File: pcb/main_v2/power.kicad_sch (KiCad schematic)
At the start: 33 parts, among them IC201 AP22811AW5-7, J201 USB_A, SW201 SW_DIP_x01, U201 LT3042xMSE

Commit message: updated schematic after review
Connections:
- net CONN-1 renamed Power Enable
- net CONN-2 renamed Power Faulty
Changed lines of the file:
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@@
 	(wire
 		(pts
-			(xy 193.04 48.26) (xy 193.04 80.01)
+			(xy 193.04 48.26) (xy 193.04 85.09)
 		)
 		(stroke
@@
 		(pts
 			(xy 43.18 128.27) (xy 43.18 138.43)
-		)
-		(stroke
-			(width 0)
-			(type default)
-		)
-	)
-	(wire
-		(pts
-			(xy 193.04 80.01) (xy 193.04 82.55)
 		)
 		(stroke
@@
 				)
 				(justify left)
-			)
-		)
-	)
-	(global_label "CONN-1"
-		(shape input)
-		(at 144.78 48.26 180)
-		(fields_autoplaced yes)
-		(effects
-			(font
-				(size 1.27 1.27)
-			)
-			(justify right)
-		)
-		(property "Intersheetrefs" "${INTERSHEET_REFS}"
-			(at 133.7514 48.26 0)
-			(hide yes)
-			(show_name no)
-			(do_not_autoplace no)
-			(effects
-				(font
-					(size 1.27 1.27)
-				)
-				(justify right)
 			)
 		)
@@
 		)
 	)
-	(global_label "CONN-2"
+	(hierarchical_label "Power Enable"
 		(shape input)
-		(at 193.04 82.55 270)
+		(at 144.78 48.26 180)
 		(fields_autoplaced yes)
 		(effects
@@
 			(justify right)
 		)
-		(property "Intersheetrefs" "${INTERSHEET_REFS}"
-			(at 193.04 93.5786 90)
-			(hide yes)
-			(show_name no)
-			(do_not_autoplace no)
-			(effects
-				(font
-					(size 1.27 1.27)
+		(property "Netzklasse" "Default"
+			(at 144.78 49.53 0)
+			(show_name no)
+			(do_not_autoplace no)
+			(effects
+				(font
+					(size 1.27 1.27)
+					(italic yes)
 				)
 				(justify right)
 			)
 		)
+	)
+	(hierarchical_label "Power Faulty"
+		(shape input)
+		(at 193.04 85.09 270)
+		(fields_autoplaced yes)
+		(effects
+			(font
+				(size 1.27 1.27)
+			)
+			(justify right)
+		)
+		(property "Netzklasse" "Default"
+			(at 194.31 85.09 90)
+			(show_name no)
+			(do_not_autoplace no)
+			(effects
+				(font
+					(size 1.27 1.27)
+					(italic yes)
+				)
+				(justify right)
+			)
+		)
+	)
+	(netclass_flag ""
+		(length 2.54)
+		(shape diamond)
+		(at 194.31 43.18 0)
+		(fields_autoplaced yes)
+		(effects
+			(font
+				(size 1.27 1.27)
+			)
+			(justify left bottom)
+		)
+		(property "Netzklasse" "Power"
+			(at 195.5165 40.64 0)
+			(show_name no)
+			(do_not_autoplace no)
+			(effects
+				(font
+					(size 1.27 1.27)
+				)
+				(justify left)
+			)
+		)
+		(property "Component Class" ""
+			(at 6.35 20.32 0)
+			(show_name no)
+			(do_not_autoplace no)
+			(effects
+				(font
+					(size 1.27 1.27)
+					(italic yes)
+				)
+			)
+		)
+	)
+	(netclass_flag ""
+		(length 2.54)
+		(shape diamond)
+		(at 173.99 128.27 0)
+		(fields_autoplaced yes)
+		(effects
+			(font
+				(size 1.27 1.27)
+			)
+			(justify left bottom)
+		)
+		(property "Netzklasse" "Power"
+			(at 175.1965 125.73 0)
+			(show_name no)
+			(do_not_autoplace no)
+			(effects
+				(font
+					(size 1.27 1.27)
+				)
+				(justify left)
+			)
+		)
+		(property "Component Class" ""
+			(at -13.97 105.41 0)
+			(show_name no)
+			(do_not_autoplace no)
+			(effects
+				(font
+					(size 1.27 1.27)
+					(italic yes)
+				)
+			)
+		)
+	)
+	(netclass_flag ""
+		(length 2.54)
+		(shape diamond)
+		(at 134.62 43.18 0)
+		(fields_autoplaced yes)
+		(effects
+			(font
+				(size 1.27 1.27)
+			)
+			(justify left bottom)
+		)
+		(property "Netzklasse" "Power"
+			(at 135.8265 40.64 0)
+			(show_name no)
+			(do_not_autoplace no)
+			(effects
+				(font
+					(size 1.27 1.27)
+				)
+				(justify left)
+			)
+		)
+		(property "Component Class" ""
+			(at -53.34 20.32 0)
+			(show_name no)
+			(do_not_autoplace no)
+			(effects
+				(font
+					(size 1.27 1.27)
+					(italic yes)
+				)
+			)
+		)

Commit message: added new osci
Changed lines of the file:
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@@
-	(wire
-		(pts
-			(xy 90.17 39.37) (xy 90.17 43.18)
-		)
-		(stroke
-			(width 0)
-			(type default)
-		)
-	)
 	(wire
 		(pts
@@
 		)
 	)
-	(global_label "USB Power"
-		(shape input)
-		(at 90.17 39.37 90)
-		(fields_autoplaced yes)
+	(label "USB Power"
+		(at 86.36 43.18 90)
 		(effects
 			(font
 				(size 1.27 1.27)
 			)
-			(justify left)
-		)
-		(property "Intersheetrefs" "${INTERSHEET_REFS}"
-			(at 90.17 25.9829 90)
-			(hide yes)
-			(show_name no)
-			(do_not_autoplace no)
-			(effects
-				(font
-					(size 1.27 1.27)
-				)
-				(justify left)
-			)
-		)
-		(property "Net Class" "Power"
-			(at 94.0118 39.37 90)
-			(show_name no)
-			(do_not_autoplace no)
-			(effects
-				(font
-					(size 1.27 1.27)
-				)
-				(justify left)
-			)
-		)
-	)
-	(global_label "USB Power"
-		(shape input)
+			(justify left bottom)
+		)
+	)
+	(label "USB Power"
 		(at 212.09 80.01 0)
-		(fields_autoplaced yes)
 		(effects
 			(font
 				(size 1.27 1.27)
 			)
-			(justify left)
-		)
-		(property "Intersheetrefs" "${INTERSHEET_REFS}"
-			(at 225.4771 80.01 0)
-			(hide yes)
-			(show_name no)
-			(do_not_autoplace no)
-			(effects
-				(font
-					(size 1.27 1.27)
-				)
-				(justify left)
-			)
+			(justify left bottom)
 		)
 	)
@@
 			)
 		)
+	)
+	(netclass_flag ""
+		(length 2.54)
+		(shape diamond)
+		(at 69.85 43.18 0)
+		(fields_autoplaced yes)
+		(effects
+			(font
+				(size 1.27 1.27)
+			)
+			(justify left bottom)
+		)
+		(property "Net Class" "Power"
+			(at 71.0565 40.64 0)
+			(show_name no)
+			(do_not_autoplace no)
+			(effects
+				(font
+					(size 1.27 1.27)
+				)
+				(justify left)
+			)
+		)
+		(property "Component Class" ""
+			(at 60.96 35.56 0)
+			(show_name no)
+			(do_not_autoplace no)
+			(effects
+				(font
+					(size 1.27 1.27)
+					(italic yes)
+				)
+			)
+		)

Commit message: updated schematic
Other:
- moved on the sheet: R202, TP202
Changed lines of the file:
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@@
+	)
+	(junction
+		(at 193.04 80.01)
+		(diameter 0)
+		(color 0 0 0 0)
+	)
+	(junction
+		(at 204.47 52.07)
+		(diameter 0)
+		(color 0 0 0 0)
+	)
+	(junction
+		(at 132.08 128.27)
+		(diameter 0)
+		(color 0 0 0 0)
+	)
+	(junction
+		(at 66.04 43.18)
+		(diameter 0)
+		(color 0 0 0 0)
+	)
+	(junction
+		(at 96.52 128.27)
+		(diameter 0)
+		(color 0 0 0 0)
+	)
+	(junction
+		(at 226.06 43.18)
+		(diameter 0)
+		(color 0 0 0 0)
+	)
+	(junction
+		(at 96.52 135.89)
+		(diameter 0)
+		(color 0 0 0 0)
+	)
+	(junction
+		(at 162.56 48.26)
+		(diameter 0)
+		(color 0 0 0 0)
+	)
+	(junction
+		(at 161.29 137.16)
+		(diameter 0)
+		(color 0 0 0 0)
 	)
 	(junction
@@
 	)
 	(junction
-		(at 193.04 80.01)
+		(at 116.84 128.27)
 		(diameter 0)
 		(color 0 0 0 0)
 	)
 	(junction
-		(at 204.47 52.07)
+		(at 157.48 43.18)
 		(diameter 0)
 		(color 0 0 0 0)
 	)
 	(junction
-		(at 132.08 128.27)
+		(at 96.52 147.32)
 		(diameter 0)
 		(color 0 0 0 0)
 	)
 	(junction
-		(at 66.04 43.18)
+		(at 161.29 128.27)
 		(diameter 0)
 		(color 0 0 0 0)
 	)
 	(junction
-		(at 96.52 128.27)
+		(at 53.34 67.31)
+		(diameter 0)
+		(color 0 0 0 0)
+	)
+	(junction
+		(at 132.08 43.18)
 		(diameter 0)
 		(color 0 0 0 0)
@@
 	)
 	(junction
-		(at 226.06 43.18)
-		(diameter 0)
-		(color 0 0 0 0)
-	)
-	(junction
-		(at 96.52 135.89)
-		(diameter 0)
-		(color 0 0 0 0)
-	)
-	(junction
-		(at 162.56 48.26)
-		(diameter 0)
-		(color 0 0 0 0)
-	)
-	(junction
-		(at 161.29 137.16)
-		(diameter 0)
-		(color 0 0 0 0)
-	)
-	(junction
-		(at 116.84 128.27)
-		(diameter 0)
-		(color 0 0 0 0)
-	)
-	(junction
-		(at 157.48 43.18)
-		(diameter 0)
-		(color 0 0 0 0)
-	)
-	(junction
-		(at 96.52 147.32)
-		(diameter 0)
-		(color 0 0 0 0)
-	)
-	(junction
-		(at 161.29 128.27)
-		(diameter 0)
-		(color 0 0 0 0)
-	)
-	(junction
-		(at 53.34 67.31)
-		(diameter 0)
-		(color 0 0 0 0)
-	)
-	(junction
-		(at 132.08 43.18)
-		(diameter 0)
-		(color 0 0 0 0)
-	)
-	(junction
-		(at 27.94 67.31)
+		(at 33.02 67.31)
 		(diameter 0)
 		(color 0 0 0 0)
@@
 	(wire
 		(pts
-			(xy 27.94 59.69) (xy 50.8 59.69)
+			(xy 33.02 59.69) (xy 50.8 59.69)
 		)
 		(stroke
@@
 	(wire
 		(pts
-			(xy 27.94 67.31) (xy 50.8 67.31)
+			(xy 33.02 67.31) (xy 50.8 67.31)
 		)
 		(stroke
@@
 	)
 	(label "Shield"
-		(at 33.02 59.69 90)
+		(at 38.1 59.69 90)
 		(fields_autoplaced yes)
 		(effects
@@
 		)
 		(property "Net Class" "GND"
-			(at 34.29 59.69 90)
+			(at 39.37 59.69 90)
 			(show_name no)
 			(do_not_autoplace no)
@@
 	(symbol
 		(lib_id "Connector:TestPoint")
-		(at 27.94 67.31 180)
+		(at 33.02 67.31 180)
 		(unit 1)
 		(body_style 1)
@@
 		(fields_autoplaced yes)
 		(property "Reference" "TP202"
-			(at 30.48 69.3419 0)
+			(at 35.56 69.3419 0)
 			(show_name no)
 			(do_not_autoplace no)
@@
 		)
 		(property "Value" "TestPoint"
-			(at 30.48 71.8819 0)
+			(at 35.56 71.8819 0)
 			(show_name no)
 			(do_not_autoplace no)
@@
 		)
 		(property "Footprint" "TestPoint:TestPoint_Pad_D1.0mm"
-			(at 22.86 67.31 0)
+			(at 27.94 67.31 0)
 			(hide yes)
 			(show_name no)
@@
 		)
 		(property "Datasheet" ""
-			(at 22.86 67.31 0)
+			(at 27.94 67.31 0)
 			(hide yes)
 			(show_name no)
@@
 		)
 		(property "Description" "test point"
-			(at 27.94 67.31 0)
+			(at 33.02 67.31 0)
 			(hide yes)
 			(show_name no)
@@
 	(symbol
 		(lib_id "Device:R")
-		(at 27.94 63.5 0)
+		(at 33.02 63.5 0)
 		(unit 1)
 		(body_style 1)
@@
 		(fields_autoplaced yes)
 		(property "Reference" "R202"
-			(at 30.48 62.2299 0)
+			(at 35.56 62.2299 0)
 			(show_name no)
 			(do_not_autoplace no)
@@
 		)
 		(property "Value" "1M"
-			(at 30.48 64.7699 0)
+			(at 35.56 64.7699 0)
 			(show_name no)
 			(do_not_autoplace no)
@@
 		)
 		(property "Footprint" "Resistor_SMD:R_0603_1608Metric"
-			(at 26.162 63.5 90)
+			(at 31.242 63.5 90)
 			(hide yes)
 			(show_name no)
@@
 		)
 		(property "Datasheet" ""
-			(at 27.94 63.5 0)
+			(at 33.02 63.5 0)
 			(hide yes)
 			(show_name no)
@@
 		)
 		(property "Description" "Resistor"
-			(at 27.94 63.5 0)
-			(hide yes)
-			(show_name no)
+			(at 33.02 63.5 0)
+			(hide yes)
+			(show_name no)

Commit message: updated pll
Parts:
- D202, D203, D204, D205: footprint LED_SMD:LED_0603_1608Metric -> LED_SMD:LED_0805_2012Metric
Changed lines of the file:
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@@
 			)
 		)
-		(property "Footprint" "LED_SMD:LED_0603_1608Metric"
+		(property "Footprint" "LED_SMD:LED_0805_2012Metric"
 			(at 246.38 46.99 0)
 			(hide yes)
@@
 			)
 		)
-		(property "Footprint" "LED_SMD:LED_0603_1608Metric"
+		(property "Footprint" "LED_SMD:LED_0805_2012Metric"
 			(at 190.5 132.08 0)
 			(hide yes)
@@
 			)
 		)
-		(property "Footprint" "LED_SMD:LED_0603_1608Metric"
+		(property "Footprint" "LED_SMD:LED_0805_2012Metric"
 			(at 208.28 80.01 0)
 			(hide yes)
@@
 			)
 		)
-		(property "Footprint" "LED_SMD:LED_0603_1608Metric"
+		(property "Footprint" "LED_SMD:LED_0805_2012Metric"
 			(at 162.56 58.42 0)
 			(hide yes)

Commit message: updarted schematic and simulation
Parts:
- removed C205: 4.7 nF, Capacitor_SMD:C_1206_3216Metric, symbol Device:C
- removed J201: USB_A, Connector_USB:USB3_A_Receptacle_Wuerth_692122030100, symbol Connector:USB_A
- removed R202: 1M, Resistor_SMD:R_0603_1608Metric, symbol Device:R
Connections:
- net USB Power renamed DC Power
- no-connect marks 2 -> 0
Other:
- note added: "Power In"
- note added: "todo: check heat power with 3.2V * i_1.8"
- note added: "todo: ferrit, netzbrummen"
- note added: "todo: power bduget überprüfen"
- note removed: "USB Power"
- moved on the sheet: D203, D204, R203, R204, R205, SW201, TP201, TP204

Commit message: improved visualization
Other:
- note added: "Imax = 200mA"
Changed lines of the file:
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@@
+		)
+	)
+	(text "Imax = 200mA"
+		(exclude_from_sim no)
+		(at 170.18 126.492 0)
+		(effects
+			(font
+				(size 1.27 1.27)
+			)
 		)
 	)

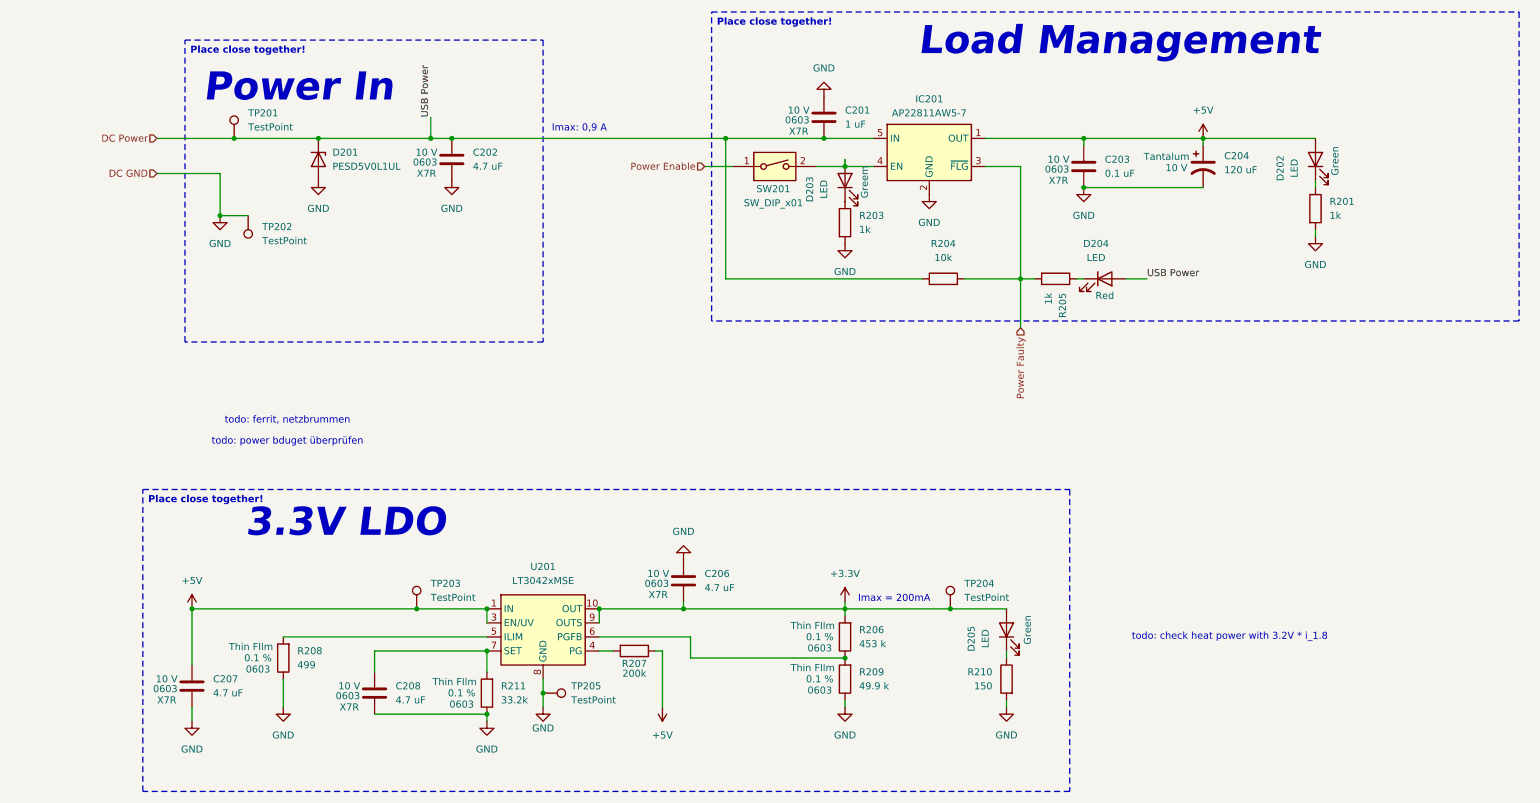
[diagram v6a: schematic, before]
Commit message: updated io schematic
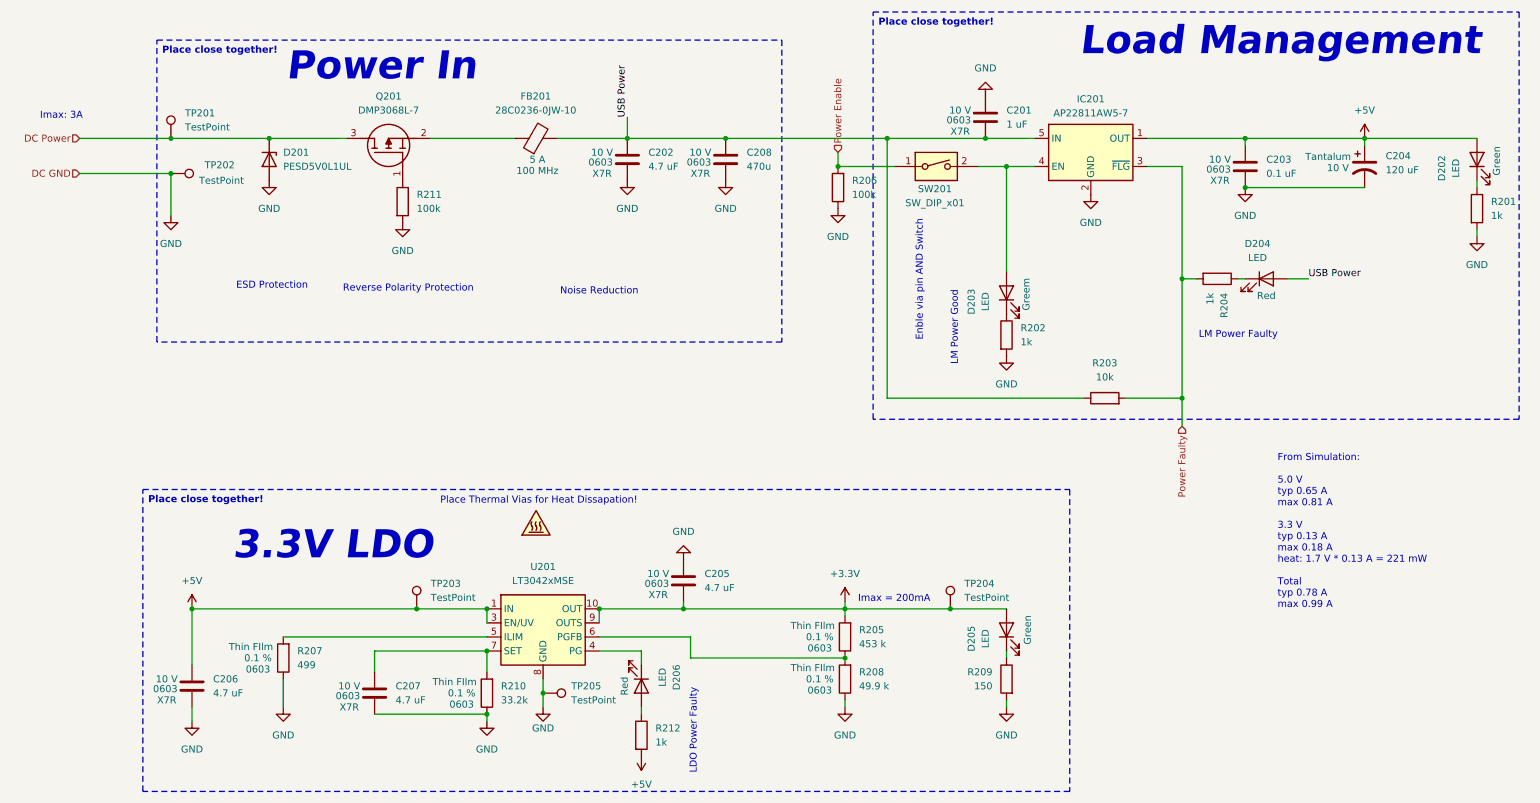
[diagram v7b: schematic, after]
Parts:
- removed R207: 200k, Resistor_SMD:R_0603_1608Metric, symbol Device:R
- added C208: 470u, Capacitor_SMD:C_0603_1608Metric, symbol Device:C
- added D206: LED, LED_SMD:LED_0805_2012Metric, symbol Device:LED
- added FB201: 28C0236-0JW-10, Ferrite_THT:LairdTech_28C0236-0JW-10, symbol Device:FerriteBead
- added Q201: DMP3068L-7, My Footprints:SOT96P240X115-3N, symbol My Symbols:DMP3068L-7
- added R206, R211: 100k, Resistor_SMD:R_0603_1608Metric, symbol Device:R
- added R212: 1k, Resistor_SMD:R_0603_1608Metric, symbol Device:R
- renumbered C206 to C205, C207 to C206, C208 to C207, R203 to R202, R204 to R203, R205 to R204, R206 to R205, R208 to R207, R209 to R208, R210 to R209, R211 to R210
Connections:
- net +5V: now also R212.2
- net DC Power: now also Q201.3 (D); no longer C201.2, C202.1, D204.2 (A), IC201.5 (IN), R203.1
- net GND: now also C208.2, R206.1, R211.2
- net Power Enable: now also R206.2
- net at U201.4 (PG): now also D206.1 (K)
- new net: Q201.1 (G), R211.1
- new net: FB201.1, Q201.2 (S)
- new net: D206.2 (A), R212.1
- new net USB Power: C201.2, C202.1, C208.1, D204.2 (A), FB201.2, IC201.5 (IN), R203.1
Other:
- note added: "ESD Protection"
- note added: "Enble via pin AND Switch"
- note added: "From Simulation: 5.0 V typ 0.65 A max 0.81 A 3.3 V typ 0.13 A max 0.18 A heat: 1.7 V * 0.13 A = 221 mW Total typ 0.78 A max 0.99 A"
- note added: "Imax: 3A"
- note added: "LDO Power Faulty"
- note added: "LM Power Faulty"
- note added: "LM Power Good"
- note added: "Noise Reduction"
- note added: "Place Thermal Vias for Heat Dissapation!"
- note added: "Reverse Polarity Protection"
- note removed: "Imax: 0,9 A"
- note removed: "todo: check heat power with 3.2V * i_1.8"
- note removed: "todo: ferrit, netzbrummen"
- note removed: "todo: power bduget überprüfen"
- moved on the sheet: C201, C202, C203, C204, D202, D203, D204, IC201, R201, R202, R203, R204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
